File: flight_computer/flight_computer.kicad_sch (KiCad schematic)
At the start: 0 parts

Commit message: can transceiver schematic
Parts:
- added U1: STM32H563RGTx, Package_QFP:LQFP-64_10x10mm_P0.5mm, symbol MCU_ST_STM32H5:STM32H563RGTx
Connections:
- new net: U1.18 (VSS), U1.31 (VSS), U1.47 (VSS), U1.63 (VSS)
- new net FDCAN1_RX: U1.44 (PA11)
- new net FDCAN1_TX: U1.45 (PA12)
- new net FDCAN2_RX: U1.33 (PB12)
- new net FDCAN2_TX: U1.34 (PB13)
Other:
- added sheet can_transceiver1 (can_transceiver.kicad_sch)
- added sheet can_transceiver2 (can_transceiver.kicad_sch)
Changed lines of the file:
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@@
 	(generator_version "10.0")
 	(paper "A4")
-	(sheet_instances
-		(path "/"
-			(page "1")
-		)
-	)
-	(embedded_fonts no)
-)

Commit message: interconnect
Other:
- added sheet interconnect (interconnect.kicad_sch)

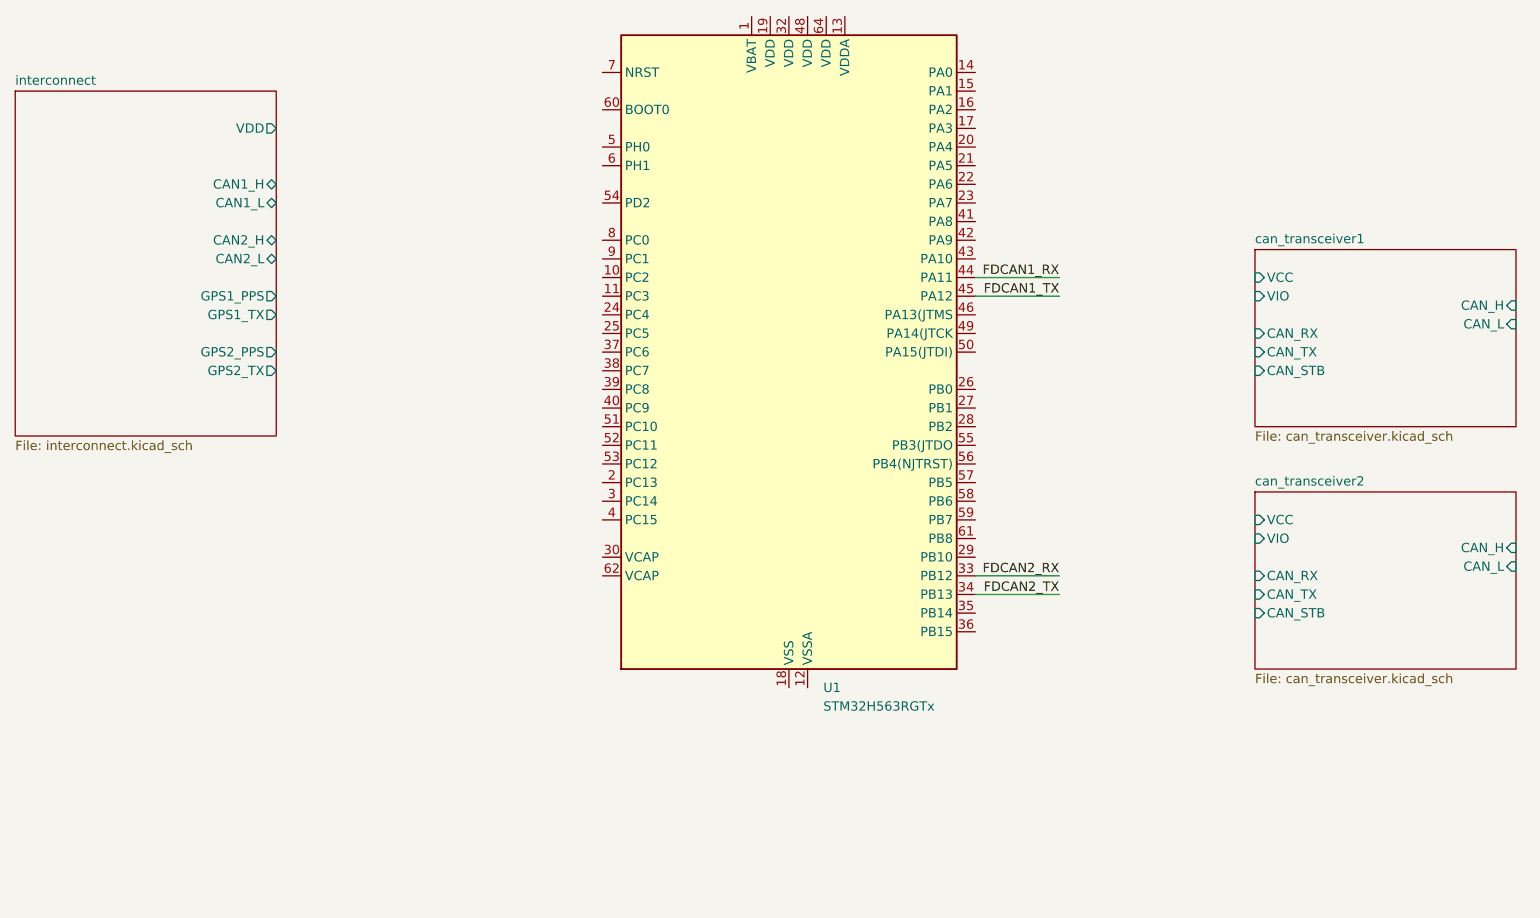
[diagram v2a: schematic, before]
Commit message: mcu clock
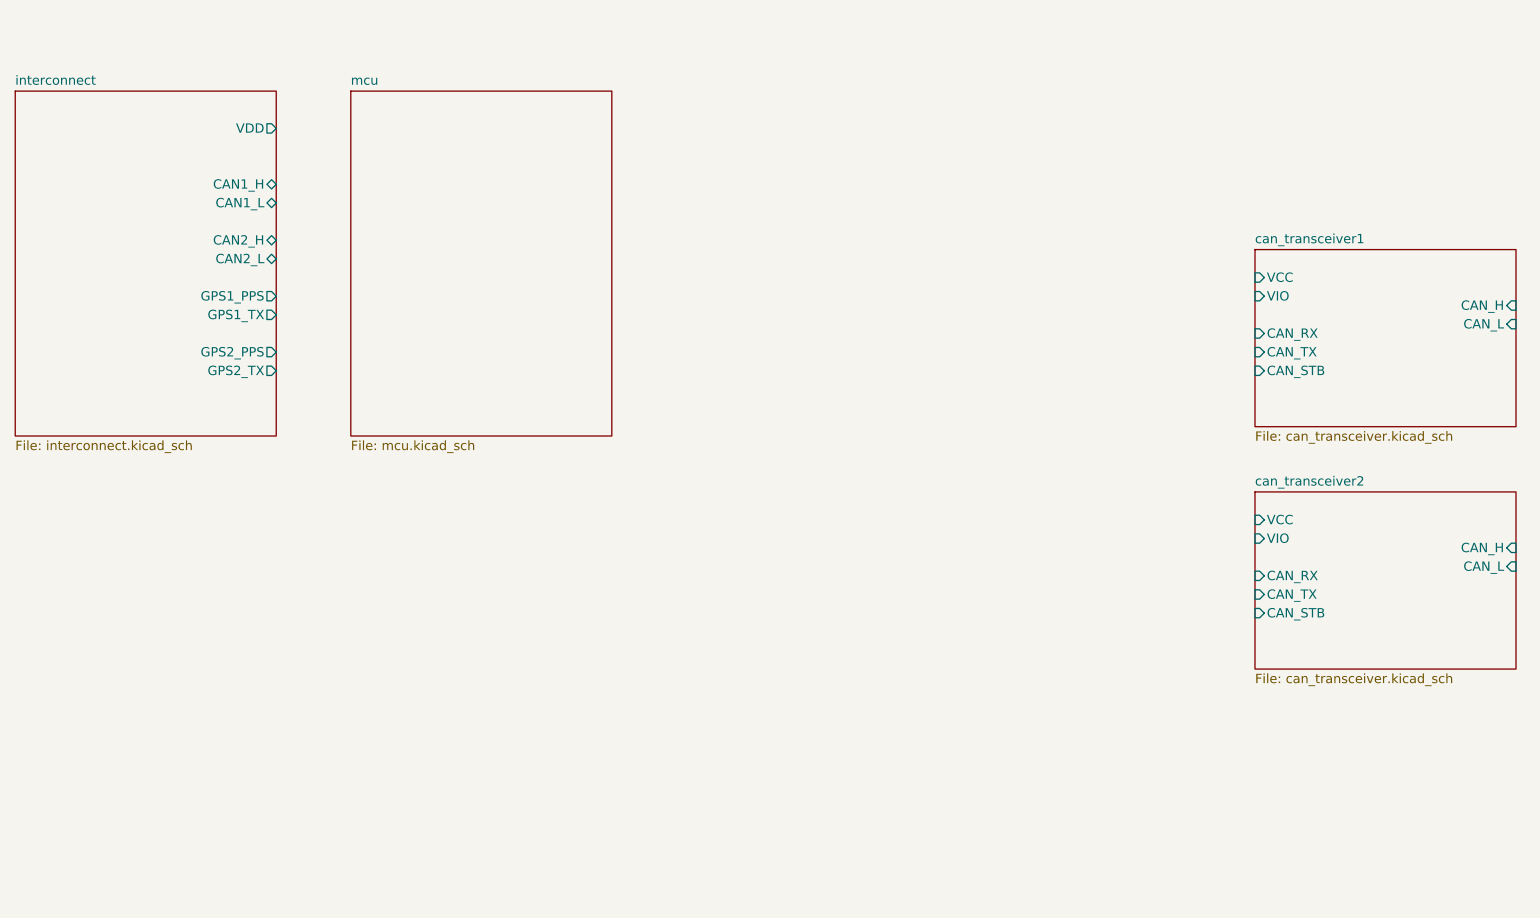
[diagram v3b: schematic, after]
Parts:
- removed U1: STM32H563RGTx, Package_QFP:LQFP-64_10x10mm_P0.5mm, symbol MCU_ST_STM32H5:STM32H563RGTx
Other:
- added sheet mcu (mcu.kicad_sch)

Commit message: flight computer mcu
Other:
- sheet mcu ports: added FDCAN1_RX, FDCAN1_TX, FDCAN2_RX, FDCAN2_TX, GPS1_PPS, GPS1_RX, GPS2_PPS, GPS2_RX, MISO, MOSI, SCK, VDD3V3; removed none
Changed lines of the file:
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@@
 	)
 	(sheet
-		(at 201.93 116.84)
+		(at 83.82 146.05)
 		(size 35.56 24.13)
 		(exclude_from_sim no)
@@
 		)
 		(property "Sheetname" "can_transceiver2"
-			(at 201.93 116.1284 0)
+			(at 83.82 145.3384 0)
 			(show_name no)
 			(do_not_autoplace no)
@@
 		)
 		(property "Sheetfile" "can_transceiver.kicad_sch"
-			(at 201.93 141.5546 0)
+			(at 83.82 170.7646 0)
 			(show_name no)
 			(do_not_autoplace no)
@@
 		)
 		(pin "CAN_RX" input
-			(at 201.93 128.27 180)
-			(effects
-				(font
-					(size 1.27 1.27)
-				)
-				(justify left)
+			(at 119.38 157.48 0)
+			(effects
+				(font
+					(size 1.27 1.27)
+				)
+				(justify right)
 			)
 		)
 		(pin "CAN_H" input
-			(at 237.49 124.46 0)
-			(effects
-				(font
-					(size 1.27 1.27)
-				)
-				(justify right)
+			(at 83.82 153.67 180)
+			(effects
+				(font
+					(size 1.27 1.27)
+				)
+				(justify left)
 			)
 		)
 		(pin "CAN_L" input
-			(at 237.49 127 0)
-			(effects
-				(font
-					(size 1.27 1.27)
-				)
-				(justify right)
+			(at 83.82 156.21 180)
+			(effects
+				(font
+					(size 1.27 1.27)
+				)
+				(justify left)
 			)
 		)
 		(pin "CAN_STB" input
-			(at 201.93 133.35 180)
-			(effects
-				(font
-					(size 1.27 1.27)
-				)
-				(justify left)
+			(at 119.38 162.56 0)
+			(effects
+				(font
+					(size 1.27 1.27)
+				)
+				(justify right)
 			)
 		)
 		(pin "CAN_TX" input
-			(at 201.93 130.81 180)
-			(effects
-				(font
-					(size 1.27 1.27)
-				)
-				(justify left)
+			(at 119.38 160.02 0)
+			(effects
+				(font
+					(size 1.27 1.27)
+				)
+				(justify right)
 			)
 		)
 		(pin "VCC" input
-			(at 201.93 120.65 180)
-			(effects
-				(font
-					(size 1.27 1.27)
-				)
-				(justify left)
+			(at 119.38 149.86 0)
+			(effects
+				(font
+					(size 1.27 1.27)
+				)
+				(justify right)
 			)
 		)
 		(pin "VIO" input
-			(at 201.93 123.19 180)
-			(effects
-				(font
-					(size 1.27 1.27)
-				)
-				(justify left)
+			(at 119.38 152.4 0)
+			(effects
+				(font
+					(size 1.27 1.27)
+				)
+				(justify right)
 			)
 		)
@@
 	)
 	(sheet
-		(at 78.74 62.23)
-		(size 35.56 46.99)
+		(at 134.62 62.23)
+		(size 35.56 78.74)
 		(exclude_from_sim no)
 		(in_bom yes)
@@
 		)
 		(property "Sheetname" "mcu"
-			(at 78.74 61.5184 0)
+			(at 134.62 61.5184 0)
 			(show_name no)
 			(do_not_autoplace no)
@@
 		)
 		(property "Sheetfile" "mcu.kicad_sch"
-			(at 78.74 109.8046 0)
+			(at 134.62 141.5546 0)
 			(show_name no)
 			(do_not_autoplace no)
@@
 				)
 				(justify left top)
+			)
+		)
+		(pin "FDCAN1_RX" input
+			(at 134.62 116.84 180)
+			(effects
+				(font
+					(size 1.27 1.27)
+				)
+				(justify left)
+			)
+		)
+		(pin "FDCAN1_TX" input
+			(at 134.62 119.38 180)
+			(effects
+				(font
+					(size 1.27 1.27)
+				)
+				(justify left)
+			)
+		)
+		(pin "GPS1_PPS" input
+			(at 134.62 90.17 180)
+			(effects
+				(font
+					(size 1.27 1.27)
+				)
+				(justify left)
+			)
+		)
+		(pin "GPS1_RX" input
+			(at 134.62 92.71 180)
+			(effects
+				(font
+					(size 1.27 1.27)
+				)
+				(justify left)
+			)
+		)
+		(pin "GPS2_PPS" input
+			(at 134.62 97.79 180)
+			(effects
+				(font
+					(size 1.27 1.27)
+				)
+				(justify left)
+			)
+		)
+		(pin "GPS2_RX" input
+			(at 134.62 100.33 180)
+			(effects
+				(font
+					(size 1.27 1.27)
+				)
+				(justify left)
+			)
+		)
+		(pin "MISO" input
+			(at 170.18 90.17 0)
+			(effects
+				(font
+					(size 1.27 1.27)
+				)
+				(justify right)
+			)
+		)
+		(pin "MOSI" input
+			(at 170.18 92.71 0)
+			(effects
+				(font
+					(size 1.27 1.27)
+				)
+				(justify right)
+			)
+		)
+		(pin "SCK" input
+			(at 170.18 95.25 0)
+			(effects
+				(font
+					(size 1.27 1.27)
+				)
+				(justify right)
+			)
+		)
+		(pin "VDD3V3" input
+			(at 134.62 67.31 180)
+			(effects
+				(font
+					(size 1.27 1.27)
+				)
+				(justify left)
+			)
+		)
+		(pin "FDCAN2_RX" input
+			(at 134.62 124.46 180)
+			(effects
+				(font
+					(size 1.27 1.27)
+				)
+				(justify left)
+			)
+		)
+		(pin "FDCAN2_TX" input
+			(at 134.62 127 180)
+			(effects
+				(font
+					(size 1.27 1.27)
+				)
+				(justify left)
 			)
 		)
@@
 	)
 	(sheet
-		(at 201.93 83.82)
+		(at 83.82 113.03)
 		(size 35.56 24.13)
 		(exclude_from_sim no)
@@
 		)
 		(property "Sheetname" "can_transceiver1"
-			(at 201.93 83.1084 0)
+			(at 83.82 112.3184 0)
 			(show_name no)
 			(do_not_autoplace no)
@@
 		)
 		(property "Sheetfile" "can_transceiver.kicad_sch"
-			(at 201.93 108.5346 0)
+			(at 83.82 137.7446 0)
 			(show_name no)
 			(do_not_autoplace no)
@@
 		)
 		(pin "CAN_RX" input
-			(at 201.93 95.25 180)
-			(effects
-				(font
-					(size 1.27 1.27)
-				)
-				(justify left)
+			(at 119.38 124.46 0)
+			(effects
+				(font
+					(size 1.27 1.27)
+				)
+				(justify right)
 			)
 		)
 		(pin "CAN_H" input
-			(at 237.49 91.44 0)
-			(effects
-				(font
-					(size 1.27 1.27)
-				)
-				(justify right)
+			(at 83.82 120.65 180)
+			(effects
+				(font
+					(size 1.27 1.27)
+				)
+				(justify left)
 			)
 		)
 		(pin "CAN_L" input
-			(at 237.49 93.98 0)
-			(effects
-				(font
-					(size 1.27 1.27)
-				)
-				(justify right)
+			(at 83.82 123.19 180)
+			(effects
+				(font
+					(size 1.27 1.27)
+				)
+				(justify left)
 			)
 		)
 		(pin "CAN_STB" input
-			(at 201.93 100.33 180)
-			(effects
-				(font
-					(size 1.27 1.27)
-				)
-				(justify left)
+			(at 119.38 129.54 0)
+			(effects
+				(font
+					(size 1.27 1.27)
+				)
+				(justify right)
 			)
 		)
 		(pin "CAN_TX" input
-			(at 201.93 97.79 180)
-			(effects
-				(font
-					(size 1.27 1.27)
-				)
-				(justify left)
+			(at 119.38 127 0)
+			(effects
+				(font
+					(size 1.27 1.27)
+				)
+				(justify right)
 			)
 		)
 		(pin "VCC" input
-			(at 201.93 87.63 180)
-			(effects
-				(font
-					(size 1.27 1.27)
-				)
-				(justify left)
+			(at 119.38 116.84 0)
+			(effects
+				(font
+					(size 1.27 1.27)
+				)
+				(justify right)
 			)
 		)
 		(pin "VIO" input
-			(at 201.93 90.17 180)
-			(effects
-				(font
-					(size 1.27 1.27)
-				)
-				(justify left)
-			)
-		)
+			(at 119.38 119.38 0)
+			(effects
+				(font
+					(size 1.27 1.27)
+				)
+				(justify right)
+			)
+		)

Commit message: flight computer power supply
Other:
- added sheet power (power.kicad_sch)
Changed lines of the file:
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@@
+		)
+	)
+	(sheet
+		(at 83.82 82.55)
+		(size 35.56 12.7)
+		(exclude_from_sim no)
+		(in_bom yes)
+		(on_board yes)
+		(dnp no)
+		(fields_autoplaced yes)
+		(stroke
+			(width 0.1524)
+			(type solid)
+		)
+		(fill
+			(color 0 0 0 0)
+		)
+		(property "Sheetname" "power"
+			(at 83.82 81.8384 0)
+			(show_name no)
+			(do_not_autoplace no)
+			(effects
+				(font
+					(size 1.27 1.27)
+				)
+				(justify left bottom)
+			)
+		)
+		(property "Sheetfile" "power.kicad_sch"
+			(at 83.82 95.8346 0)
+			(show_name no)
+			(do_not_autoplace no)
+			(effects
+				(font
+					(size 1.27 1.27)
+				)
+				(justify left top)
+			)
+		)
+		(pin "3V3_LDO" output
+			(at 119.38 91.44 0)
+			(effects
+				(font
+					(size 1.27 1.27)
+				)
+				(justify right)
+			)
+		)
+		(pin "VDD" input
+			(at 83.82 86.36 180)
+			(effects
+				(font
+					(size 1.27 1.27)
+				)
+				(justify left)
+			)
+		)
+		(pin "VDD3V3" output
+			(at 119.38 86.36 0)
+			(effects
+				(font
+					(size 1.27 1.27)
+				)
+				(justify right)
+			)
+		)
+		(instances
+			(project "flight_computer"
+				(path "/4b3676e8-35c3-4ec2-859c-99a6df767b3c"
+					(page "6")
+				)
+			)
 		)
 	)
